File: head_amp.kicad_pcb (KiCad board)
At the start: 4 copper layers, 50 x 50 mm, 79 parts, among them J1 USB Port, J2 I2C, J3 LED, J4 Left_Mic, J5 Left_Speaker, J6 Right_Mic, J7 Right_Speaker, J8 Fan, Q1 MMBT3904, Q2 MMBT3904, Q3 AO3401A, Q4 AO3400A, SW1 SW_Push, SW2 SW_Push, U1 AMS1117-3.3, U2 CH340K, U4 Headphone Jack, U5 WM8988LGECN/V, U6 WM8988LGECN/V, U7 AMS1117-3.3, U8 ESP32-WROOM-32E

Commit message: Update head_amp.kicad_pcb
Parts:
- moved C13 1.00 mm to (159.0, 79.0)
- moved C14 1.00 mm to (159.0, 81.5)
- moved C17 1.00 mm to (154.0, 81.5)
- moved C18 1.00 mm to (154.0, 79.0)
- moved C26 1.00 mm to (142.0, 79.0)
- moved C27 1.00 mm to (142.0, 81.5)
- moved C30 1.00 mm to (137.0, 81.5)
- moved C31 1.00 mm to (137.0, 79.0)
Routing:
- net Net-(U6-LOUT1): track 13.0 -> 11.7 mm
- net Net-(U6-ROUT1): track 11.6 -> 10.5 mm
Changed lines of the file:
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@@
 	(footprint "Capacitor_SMD:C_1206_3216Metric"
 		(layer "F.Cu")
-		(at 136.975 80.5 180)
+		(at 136.975 81.5 180)
 		(descr "Capacitor SMD 1206 (3216 Metric), square (rectangular) end terminal, IPC-7351 nominal, (Body size source: IPC-SM-782 page 76, https://www.pcb-3d.com/wordpress/wp-content/uploads/ipc-sm-782a_amendment_1_and_2.pdf), generated with kicad-footprint-generator")
 		(tags "capacitor")
@@
 	(footprint "Capacitor_SMD:C_1206_3216Metric"
 		(layer "F.Cu")
-		(at 159.025 80.5 180)
+		(at 159.025 81.5 180)
 		(descr "Capacitor SMD 1206 (3216 Metric), square (rectangular) end terminal, IPC-7351 nominal, (Body size source: IPC-SM-782 page 76, https://www.pcb-3d.com/wordpress/wp-content/uploads/ipc-sm-782a_amendment_1_and_2.pdf), generated with kicad-footprint-generator")
 		(tags "capacitor")
@@
 	(footprint "Capacitor_SMD:C_1206_3216Metric"
 		(layer "F.Cu")
-		(at 159.025 78 180)
+		(at 159.025 79 180)
 		(descr "Capacitor SMD 1206 (3216 Metric), square (rectangular) end terminal, IPC-7351 nominal, (Body size source: IPC-SM-782 page 76, https://www.pcb-3d.com/wordpress/wp-content/uploads/ipc-sm-782a_amendment_1_and_2.pdf), generated with kicad-footprint-generator")
 		(tags "capacitor")
@@
 	(footprint "Capacitor_SMD:C_1206_3216Metric"
 		(layer "F.Cu")
-		(at 136.975 78 180)
+		(at 136.975 79 180)
 		(descr "Capacitor SMD 1206 (3216 Metric), square (rectangular) end terminal, IPC-7351 nominal, (Body size source: IPC-SM-782 page 76, https://www.pcb-3d.com/wordpress/wp-content/uploads/ipc-sm-782a_amendment_1_and_2.pdf), generated with kicad-footprint-generator")
 		(tags "capacitor")
@@
 	(footprint "Capacitor_SMD:C_1206_3216Metric"
 		(layer "F.Cu")
-		(at 153.975 78 180)
+		(at 153.975 79 180)
 		(descr "Capacitor SMD 1206 (3216 Metric), square (rectangular) end terminal, IPC-7351 nominal, (Body size source: IPC-SM-782 page 76, https://www.pcb-3d.com/wordpress/wp-content/uploads/ipc-sm-782a_amendment_1_and_2.pdf), generated with kicad-footprint-generator")
 		(tags "capacitor")
@@
 	(footprint "Capacitor_SMD:C_1206_3216Metric"
 		(layer "F.Cu")
-		(at 142.025 80.5 180)
+		(at 142.025 81.5 180)
 		(descr "Capacitor SMD 1206 (3216 Metric), square (rectangular) end terminal, IPC-7351 nominal, (Body size source: IPC-SM-782 page 76, https://www.pcb-3d.com/wordpress/wp-content/uploads/ipc-sm-782a_amendment_1_and_2.pdf), generated with kicad-footprint-generator")
 		(tags "capacitor")
@@
 	(footprint "Capacitor_SMD:C_1206_3216Metric"
 		(layer "F.Cu")
-		(at 153.975 80.5 180)
+		(at 153.975 81.5 180)
 		(descr "Capacitor SMD 1206 (3216 Metric), square (rectangular) end terminal, IPC-7351 nominal, (Body size source: IPC-SM-782 page 76, https://www.pcb-3d.com/wordpress/wp-content/uploads/ipc-sm-782a_amendment_1_and_2.pdf), generated with kicad-footprint-generator")
 		(tags "capacitor")
@@
 	(footprint "Capacitor_SMD:C_1206_3216Metric"
 		(layer "F.Cu")
-		(at 142.025 78 180)
+		(at 142.025 79 180)
 		(descr "Capacitor SMD 1206 (3216 Metric), square (rectangular) end terminal, IPC-7351 nominal, (Body size source: IPC-SM-782 page 76, https://www.pcb-3d.com/wordpress/wp-content/uploads/ipc-sm-782a_amendment_1_and_2.pdf), generated with kicad-footprint-generator")
 		(tags "capacitor")
@@
 	)
 	(segment
-		(start 142.5 81.190448)
-		(end 143.309552 82)
+		(start 143.309552 83)
+		(end 145 83)
 		(width 0.3)
 		(layer "F.Cu")
@@
 	)
 	(segment
-		(start 138.45 78)
-		(end 139.601 76.849)
+		(start 142.5 79.259552)
+		(end 142.5 82.190448)
 		(width 0.3)
 		(layer "F.Cu")
@@
 	)
 	(segment
-		(start 145 82)
-		(end 150.2 87.2)
+		(start 146.646 84.646)
+		(end 147.73237 84.646)
 		(width 0.3)
 		(layer "F.Cu")
@@
 	)
 	(segment
-		(start 142.5 78.259552)
-		(end 142.5 81.190448)
+		(start 141.089448 77.849)
+		(end 142.5 79.259552)
 		(width 0.3)
 		(layer "F.Cu")
@@
 	)
 	(segment
-		(start 143.309552 82)
-		(end 145 82)
+		(start 150.2 87.11363)
+		(end 150.2 88.245)
 		(width 0.3)
 		(layer "F.Cu")
@@
 	)
 	(segment
-		(start 150.2 87.2)
-		(end 150.2 88.245)
+		(start 139.601 77.849)
+		(end 141.089448 77.849)
+		(width 0.3)
+		(layer "F.Cu")
+		(net 7)
+	)
+	(segment
+		(start 145 83)
+		(end 146.646 84.646)
+		(width 0.3)
+		(layer "F.Cu")
+		(net 7)
+	)
+	(segment
+		(start 138.45 79)
+		(end 138.45 81.5)
 		(width 0.3)
 		(layer "F.Cu")
@@
 	)
 	(segment
-		(start 138.45 78)
-		(end 138.45 80.5)
+		(start 138.45 79)
+		(end 139.601 77.849)
 		(width 0.3)
 		(layer "F.Cu")
@@
 	)
 	(segment
-		(start 141.089448 76.849)
-		(end 142.5 78.259552)
+		(start 147.73237 84.646)
+		(end 150.2 87.11363)
 		(width 0.3)
 		(layer "F.Cu")
@@
 	)
 	(segment
-		(start 139.601 76.849)
-		(end 141.089448 76.849)
+		(start 142.5 82.190448)
+		(end 143.309552 83)
 		(width 0.3)
 		(layer "F.Cu")
@@
 	)
 	(segment
-		(start 143.5 78)
-		(end 143.5 80.5)
+		(start 143.5 79)
+		(end 143.5 81.5)
 		(width 0.3)
 		(layer "F.Cu")
@@
 	)
 	(segment
-		(start 143.5 80.5)
-		(end 146.455 80.5)
+		(start 143.5 81.5)
+		(end 144.5 81.5)
 		(width 0.3)
 		(layer "F.Cu")
@@
 	)
 	(segment
-		(start 146.455 80.5)
+		(start 144.5 81.5)
+		(end 147.245 84.245)
+		(width 0.3)
+		(layer "F.Cu")
+		(net 8)
+	)
+	(segment
+		(start 147.245 84.245)
 		(end 150.2 84.245)
 		(width 0.3)
@@
 	)
 	(segment
-		(start 157.55 78)
-		(end 157.55 80.5)
+		(start 157.55 79)
+		(end 157.55 81.5)
 		(width 0.3)
 		(layer "F.Cu")
@@
 	)
 	(segment
+		(start 158.55 81.5)
+		(end 157.55 81.5)
+		(width 0.3)
+		(layer "F.Cu")
+		(net 10)
+	)
+	(segment
 		(start 160.502 87.691398)
 		(end 160.502 83.452)
@@
 	(segment
 		(start 160.502 83.452)
-		(end 157.55 80.5)
+		(end 158.55 81.5)
 		(width 0.3)
 		(layer "F.Cu")
@@
 	)
 	(segment
-		(start 159.785597 87.840701)
-		(end 160.101 87.525298)
+		(start 158.960943 82.651)
+		(end 153.651 82.651)
 		(width 0.3)
 		(layer "F.Cu")
@@
 	)
 	(segment
-		(start 159.390699 87.840701)
-		(end 159.785597 87.840701)
+		(start 153.651 82.651)
+		(end 152.5 81.5)
 		(width 0.3)
 		(layer "F.Cu")
@@
 	)
 	(segment
-		(start 160.101 83.791057)
-		(end 157.960943 81.651)
+		(start 160.101 87.525298)
+		(end 160.101 83.791057)
 		(width 0.3)
 		(layer "F.Cu")
@@
 	)
 	(segment
-		(start 157.960943 81.651)
-		(end 153.651 81.651)
+		(start 159.390699 87.840701)
+		(end 159.785597 87.840701)
 		(width 0.3)
 		(layer "F.Cu")
@@
 	)
 	(segment
-		(start 160.101 87.525298)
-		(end 160.101 83.791057)
+		(start 159.785597 87.840701)
+		(end 160.101 87.525298)
 		(width 0.3)
 		(layer "F.Cu")
@@
 	)
 	(segment
-		(start 153.651 81.651)
-		(end 152.5 80.5)
+		(start 160.101 83.791057)
+		(end 158.960943 82.651)
 		(width 0.3)
 		(layer "F.Cu")
@@
 	)
 	(segment
-		(start 152.5 78)
-		(end 152.5 80.5)
+		(start 152.5 79)
+		(end 152.5 81.5)
 		(width 0.3)
 		(layer "F.Cu")
@@
 	)
 	(segment
-		(start 161.5 81.5)
+		(start 160.5 81.5)
 		(end 164 81.5)
 		(width 0.3)
@@
 	)
 	(segment
-		(start 160.5 80.5)
-		(end 161.5 81.5)
-		(width 0.3)
-		(layer "F.Cu")
-		(net 33)
-	)
-	(segment
 		(start 165.9675 83.4675)
 		(end 165.9675 87.25)
@@
 	)
 	(segment
-		(start 160.5 78)
-		(end 160.5 80.5)
+		(start 160.5 79)
+		(end 160.5 81.5)
 		(width 0.3)
 		(layer "F.Cu")
@@
 	)
 	(segment
-		(start 164.0665 76.849)
-		(end 165.9675 78.75)
+		(start 155.45 79)
+		(end 156.601 77.849)
 		(width 0.3)
 		(layer "F.Cu")
@@
 	)
 	(segment
-		(start 155.45 78)
-		(end 156.601 76.849)
+		(start 165.0665 77.849)
+		(end 165.9675 78.75)
 		(width 0.3)
 		(layer "F.Cu")
@@
 	)
 	(segment
-		(start 155.45 78)
-		(end 155.45 80.5)
+		(start 155.45 79)
+		(end 155.45 81.5)
 		(width 0.3)
 		(layer "F.Cu")
@@
 	)
 	(segment
-		(start 156.601 76.849)
-		(end 164.0665 76.849)
+		(start 156.601 77.849)
+		(end 165.0665 77.849)
 		(width 0.3)
 		(layer "F.Cu")
@@
 	)
 	(segment
-		(start 139.5 82.5)
-		(end 139.5 81.55)
+		(start 140.55 81.5)
+		(end 140.55 79)
 		(width 0.3)
 		(layer "F.Cu")
@@
 	)
 	(segment
-		(start 140.55 80.5)
-		(end 140.55 78)
+		(start 139.502 82.548)
+		(end 140.55 81.5)
 		(width 0.3)
 		(layer "F.Cu")
@@
 	)
 	(segment
-		(start 139.011 88.2907)
-		(end 139.502 87.7997)
-		(width 0.3)
-		(layer "F.Cu")
-		(net 57)
-	)
-	(segment
 		(start 139.502 87.7997)
-		(end 139.502 82.502)
-		(width 0.3)
-		(layer "F.Cu")
-		(net 57)
-	)
-	(segment
-		(start 139.5 81.55)
-		(end 140.55 80.5)
+		(end 139.502 82.548)
 		(width 0.3)
 		(layer "F.Cu")
@@
 	)
 	(segment
-		(start 139.502 82.502)
-		(end 139.5 82.5)
+		(start 139.011 88.2907)
+		(end 139.502 87.7997)
 		(width 0.3)
 		(layer "F.Cu")
@@
 	)
 	(segment
-		(start 135.5 78)
-		(end 135.5 80.5)
-		(width 0.3)
-		(layer "F.Cu")
-		(net 59)
-	)
-	(segment
-		(start 139.101 83.791057)
-		(end 138.309943 83)
+		(start 135.5 79)
+		(end 135.5 81.5)
 		(width 0.3)
 		(layer "F.Cu")
@@
 	)
 	(segment
-		(start 136.5 83)
-		(end 135.5 82)
+		(start 138.390699 87.840701)
+		(end 138.893899 87.840701)
 		(width 0.3)
 		(layer "F.Cu")
@@
 	)
 	(segment
-		(start 138.390699 87.840701)
-		(end 138.893899 87.840701)
+		(start 137 83)
+		(end 135.5 81.5)
 		(width 0.3)
 		(layer "F.Cu")
@@
 	)
 	(segment
-		(start 135.5 82)
-		(end 135.5 80.5)
+		(start 138.309943 83)
+		(end 137 83)
 		(width 0.3)
 		(layer "F.Cu")
@@
 	)
 	(segment
-		(start 138.309943 83)
-		(end 136.5 83)
+		(start 139.101 83.791057)
+		(end 138.309943 83)
 		(width 0.3)
 		(layer "F.Cu")

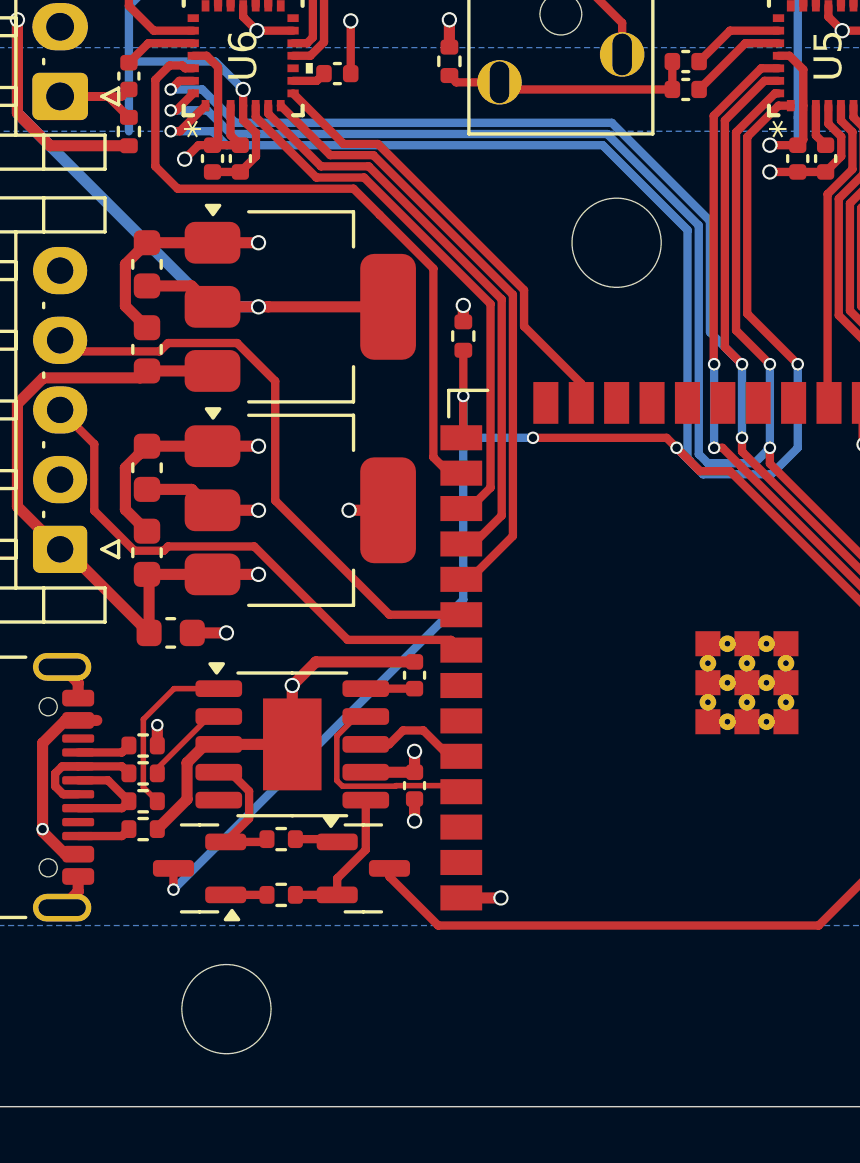
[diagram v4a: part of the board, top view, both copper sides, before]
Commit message: Add holes and generic control button
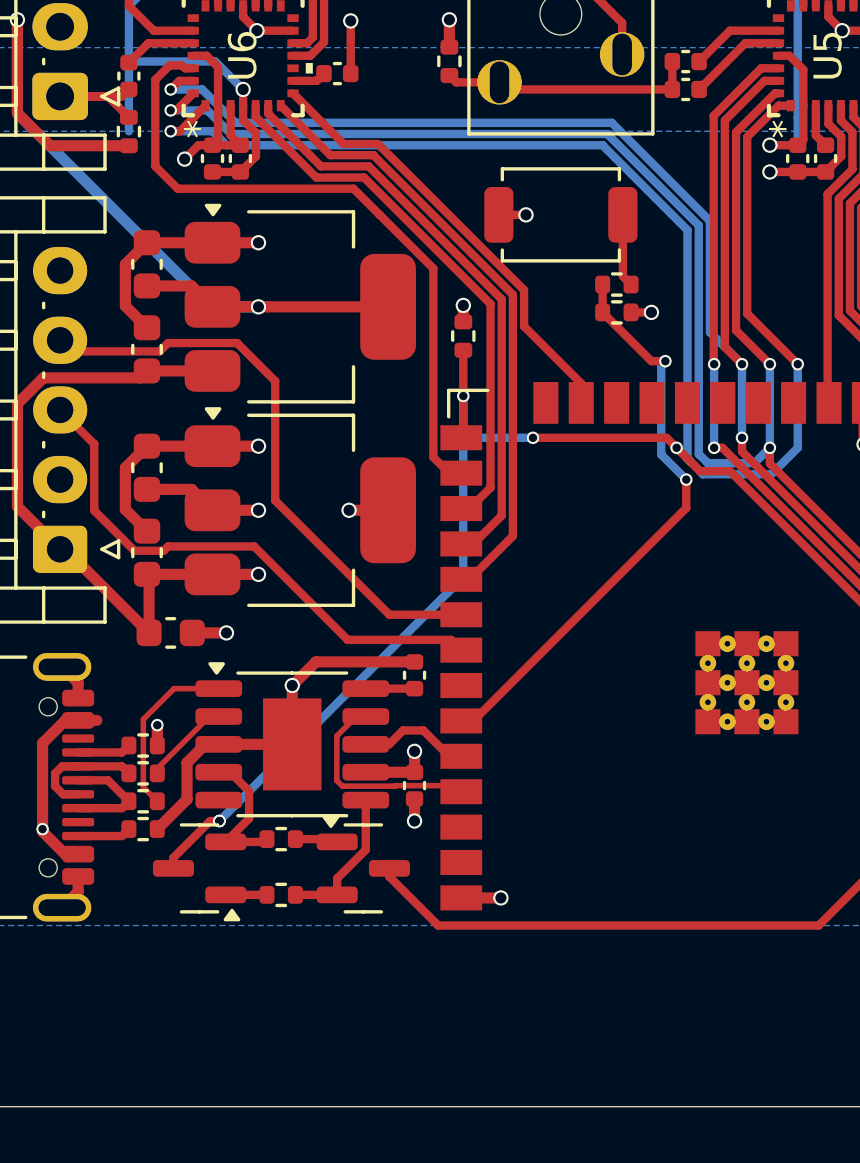
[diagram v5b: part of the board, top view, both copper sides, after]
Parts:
- removed H1, H6: MountingHole, MountingHole:MountingHole_3.2mm_M3
- added R11: 1k, Resistor_SMD:R_0402_1005Metric, F.Cu at (150.0, 96.5)
- added R7: 51k, Resistor_SMD:R_0402_1005Metric, F.Cu at (150.0, 97.5)
- added SW3: SW_Push, Button_Switch_SMD:SW_SPST_TS-1088-xR020, F.Cu at (148.0, 94.0)
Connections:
- U8 pad 33: unconnected-(U8-IO21-Pad33) -> /Gen_Button
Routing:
- net /Gen_Button: track 0.00 -> 20.9 mm, vias 0 -> 2
- net Net-(R11-Pad1): track 0.00 -> 2.62 mm
- net /GPIO0: track 106.0 -> 104.7 mm, vias 8 -> 9
- net GND: track 98.5 -> 99.8 mm, vias 16 -> 17
- net +3V3D: track 29.8 -> 30.6 mm, vias 7 -> 8
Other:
- board text added: "Boot"
- board text added: "En"

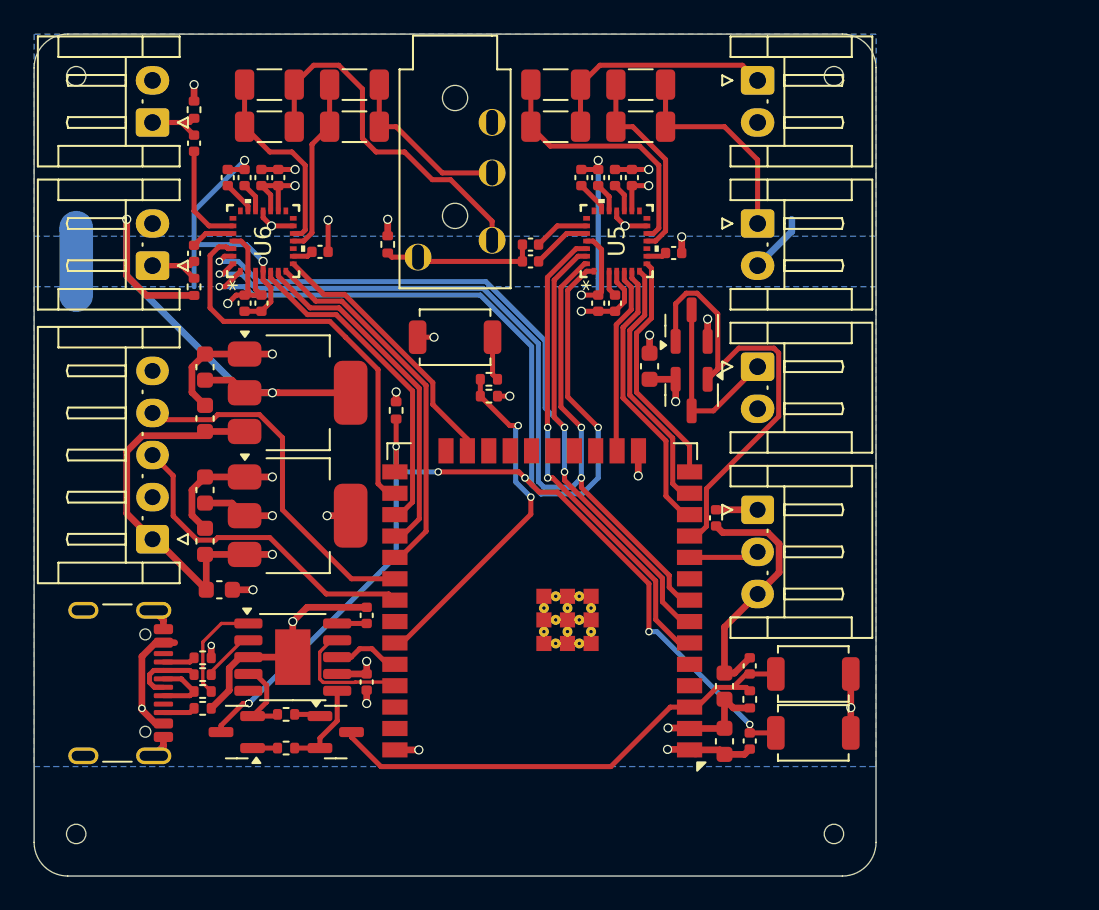
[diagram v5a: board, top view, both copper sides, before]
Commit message: Add second expansion port
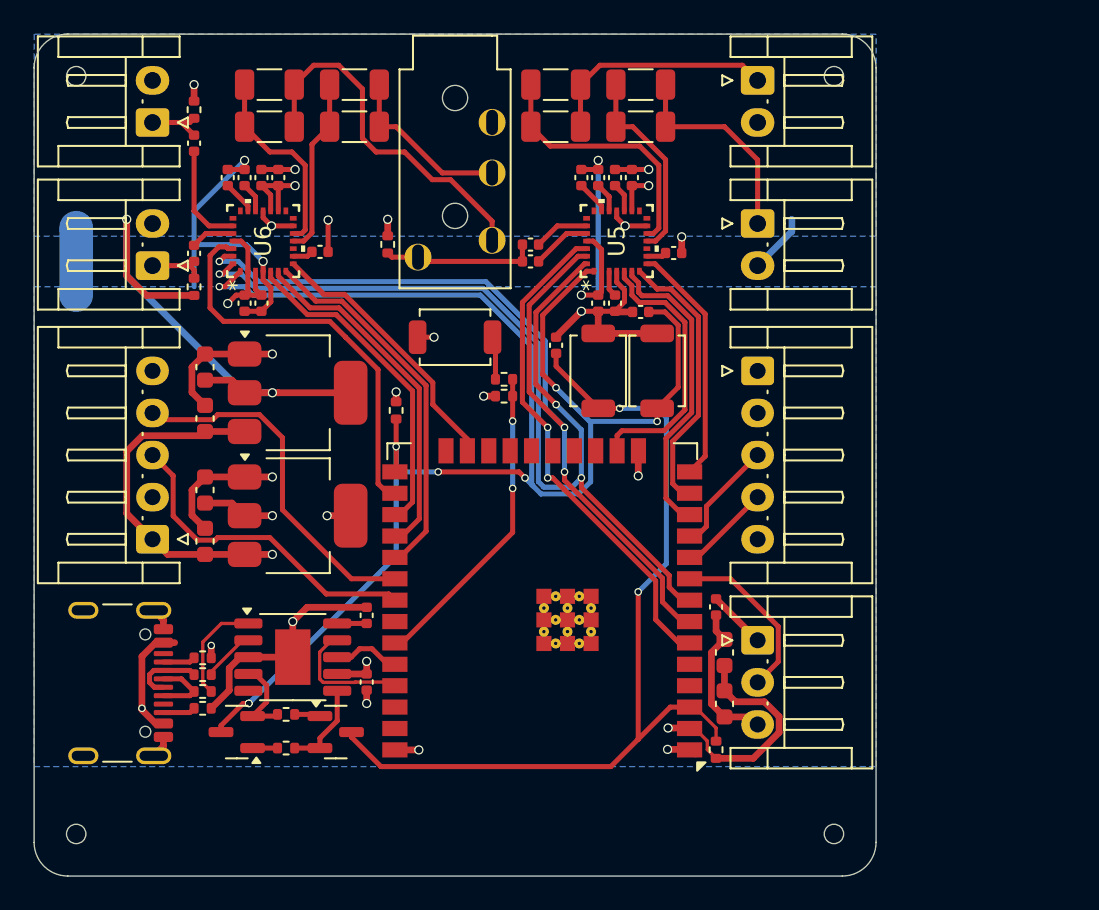
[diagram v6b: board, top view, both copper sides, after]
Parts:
- removed C2, C38: 100n, Capacitor_SMD:C_0603_1608Metric
- removed Q3: AO3401A, Package_TO_SOT_SMD:SOT-23
- removed Q4: AO3400A, Package_TO_SOT_SMD:SOT-23
- J8: value Fan -> I2C; footprint Connector_JST:JST_EH_S2B-EH_1x02_P2.50mm_Horizontal -> Connector_JST:JST_EH_S5B-EH_1x05_P2.50mm_Horizontal
- moved C7 26.3 mm to (159.0, 92.5), turned to 0 degrees
- moved SW1 23.4 mm to (160.0, 96.0), turned to -90 degrees
- moved C8 22.2 mm to (154.0, 94.5)
- moved SW2 22.1 mm to (156.5, 96.0), turned to -90 degrees
- moved J3 7.75 mm to (166.0, 112.0)
- moved C4 5.29 mm to (163.5, 110.0)
- moved C9 5.28 mm to (164.0, 112.7), turned to -90 degrees
- moved R13 3.60 mm to (163.5, 118.5)
- moved C10 1.05 mm to (164.0, 115.8), turned to -90 degrees
- moved R11 0.90 mm to (150.9, 96.5), turned to 0 degrees
- moved R7 0.90 mm to (150.9, 97.5), turned to 180 degrees
- moved J8 0.25 mm to (166.0, 96.0)
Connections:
- net /Out_CLK renamed /Out_CLK1
- net /Out_DAT renamed /Out_DAT1
- J8 pad 1: Net-(J8-Pin_1) -> +5V
- J8 pad 2: GND -> +3V3D
- U8 pad 10: /LED_Data -> /Out_CLK2
- U8 pad 11: /Fan_PWM -> /Out_DAT2
- U8 pad 9: unconnected-(U8-IO33-Pad9) -> /LED_Data
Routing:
- net /Fan_PWM: track 28.1 -> 0.00 mm
- net /MCU_EN: track 29.7 -> 54.0 mm, vias 0 -> 2
- net Net-(J8-Pin_1): track 11.0 -> 0.00 mm
- net /GPIO0: track 104.7 -> 94.7 mm, vias 9 -> 8
- net GND: track 99.8 -> 90.8 mm, vias 17 -> 13
- net +3V3D: track 30.6 -> 38.3 mm
- net /Out_DAT2: track 0.00 -> 6.73 mm
- net /LED_Data: track 4.18 -> 10.3 mm
- net /Out_CLK2: track 0.00 -> 5.52 mm
- net /Int->Ext_CLK: track 11.4 -> 16.4 mm
- net +5V: track 36.3 -> 31.7 mm, vias 3 -> 2
- net /Gen_Button: track 20.9 -> 18.8 mm
- net /Mic_Left: track 5.35 -> 3.42 mm
- net /Int->Ext_In: track 16.8 -> 18.3 mm
- net /SPI_CLK: track 56.9 -> 58.2 mm
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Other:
- board text added: "Expansion 1"
- board text added: "Expansion 2"
- board text removed: "Boot"
- board text removed: "En"
- board text removed: "Fan"
- board text removed: "I2C"
